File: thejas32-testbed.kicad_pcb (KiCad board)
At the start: 4 copper layers, 81.4 x 89.2 mm, 101 parts, among them J1 Conn_01x04, J10 Conn_02x10_Odd_Even, J11 Conn_01x03, J12 Conn_02x20_Odd_Even, J13 Conn_01x03, J2 USB_B_Micro, J3 Conn_02x03_Odd_Even, J4 Conn_02x05_Odd_Even, J5 Conn_01x05, J6 Conn_01x10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

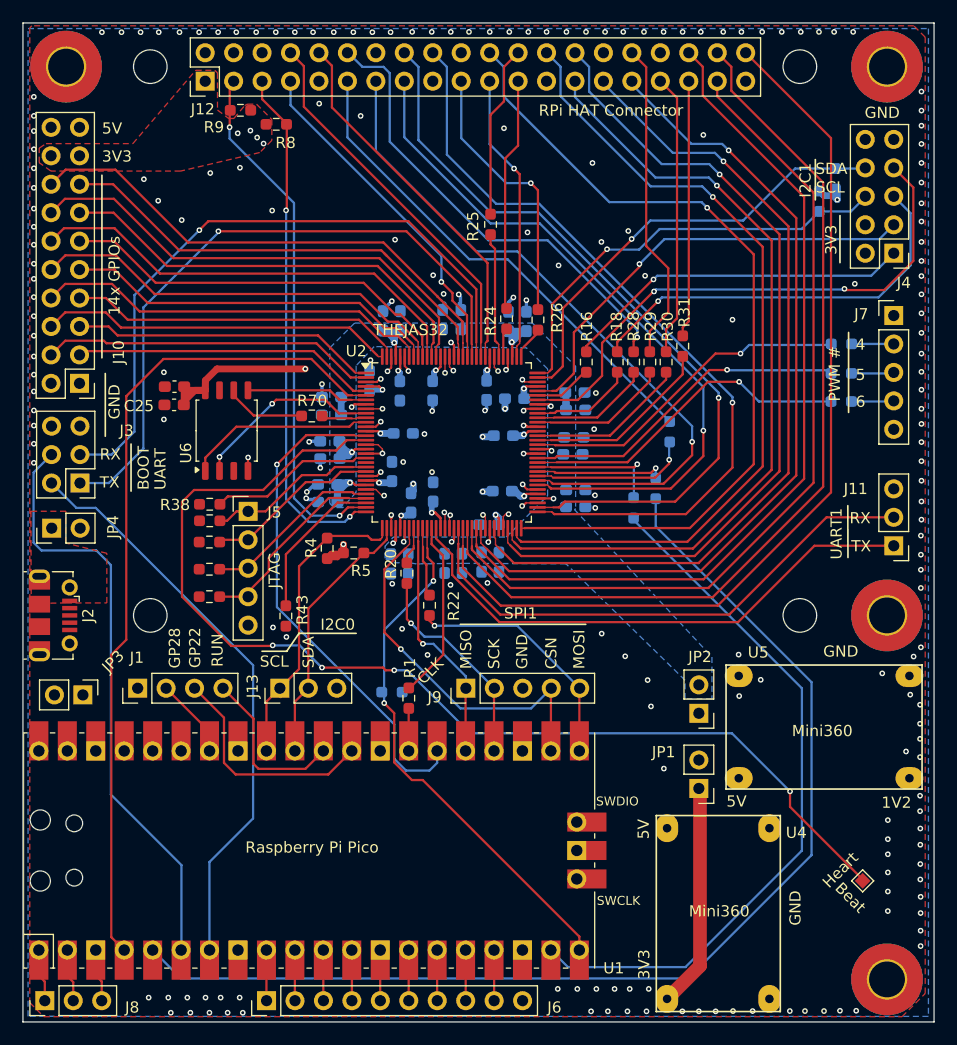
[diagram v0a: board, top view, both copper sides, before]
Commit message: Address review comments from Atharva
Various changes:
1. Deleted GND via near R9
2. Added vias near corner mounting holes
3. Thermal spoke width 40 mils for PWR_5V
   on 3rd layer
4. Fix square trace near J10.19
5. GND shapes on all planes - change to
   relief for PTH. Spoke width 20 mils
6. U1.26 routed trace above through-hole
   pafs
7. Improved routing of MCU_RESETN and
   HEARTBEAT for better GND shapes
8. U1.1-3 adjust traces to leave pad at
   90 degree

Plus silkscreen mods, including author,
version, name AtiVEGA and open hardware logo.
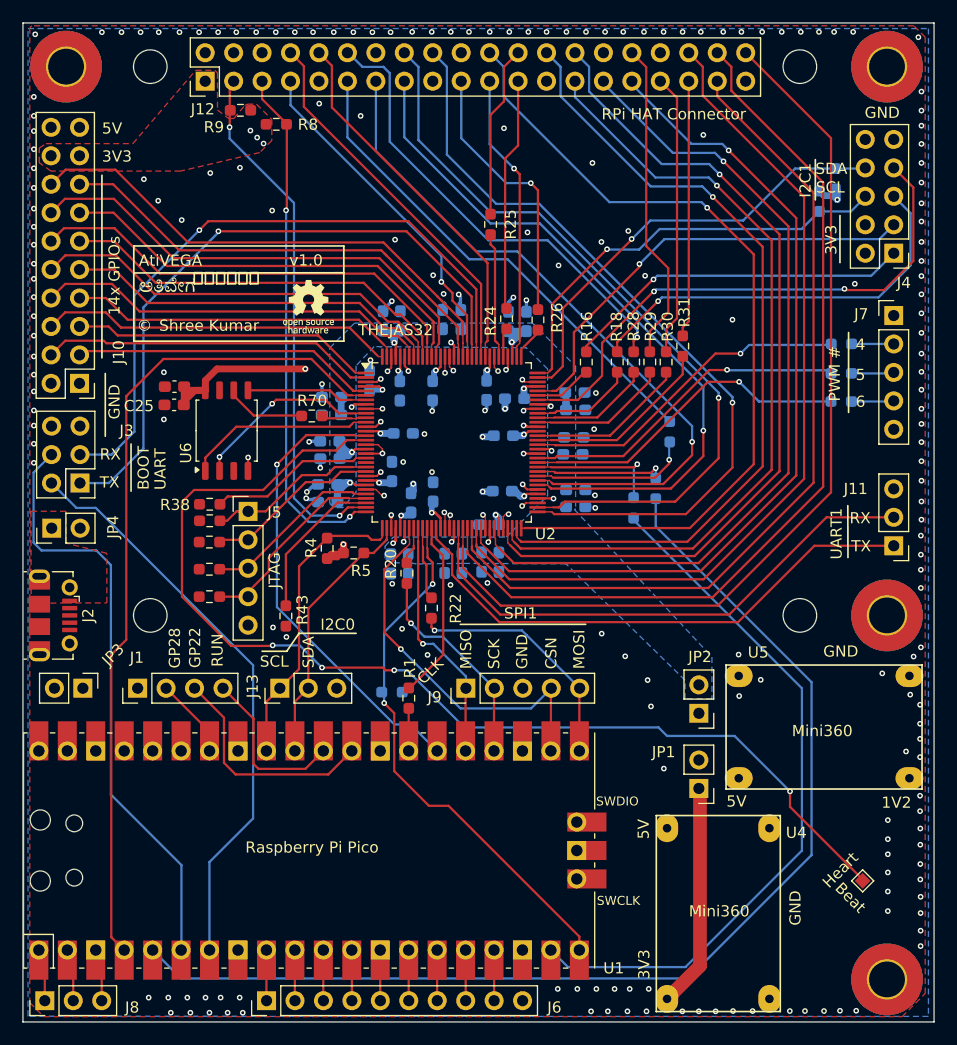
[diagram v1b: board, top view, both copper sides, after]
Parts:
- moved JP3 0.60 mm to (122.6, 126.0)
- moved R22 0.30 mm to (153.7, 118.8)
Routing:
- net MCU_BOOT_SEL: track 45.3 -> 41.4 mm
- net PWR_5V: track 140.8 -> 144.1 mm
- net Net-(JP3-B): track 5.58 -> 6.18 mm
- net GND: vias 232 -> 233
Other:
- board text added: "AtiVEGA"
- board text added: "Shree Kumar"
- board text added: "v1.0"
- board text added: "©"
- board text added: "ಅತಿವೇಗ"

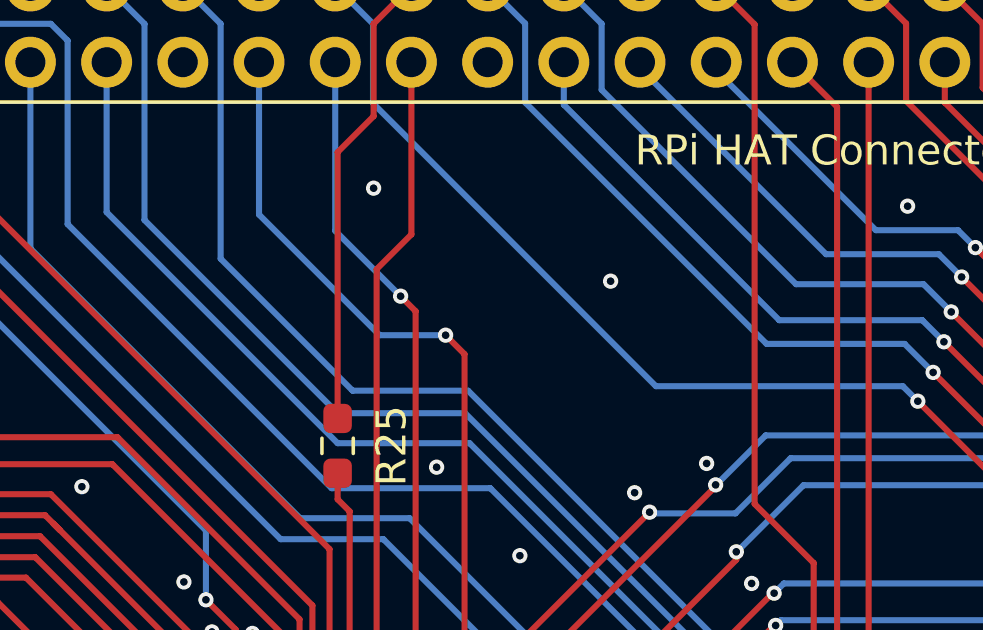
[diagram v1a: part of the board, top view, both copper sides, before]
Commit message: PCB and Silkscreen improvements
Added a couple of vias to create grounds between
traces. Moved a couple of traces to improve ground
near Pico.

Added github link as QR code on bottom silk
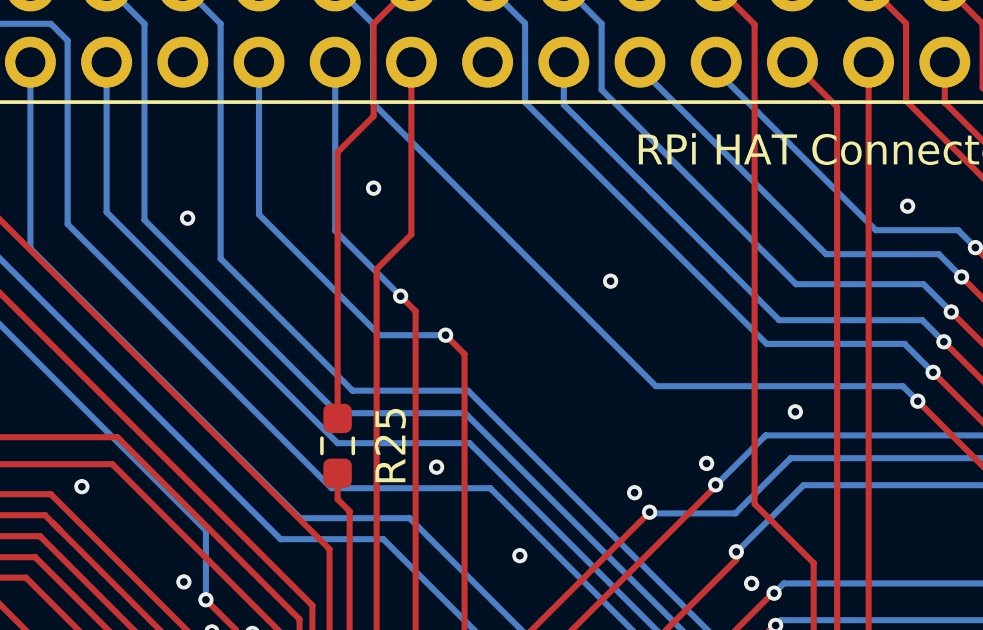
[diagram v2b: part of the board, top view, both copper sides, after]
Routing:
- net GND: vias 233 -> 235
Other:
- board text removed: "BOOT_SEL"

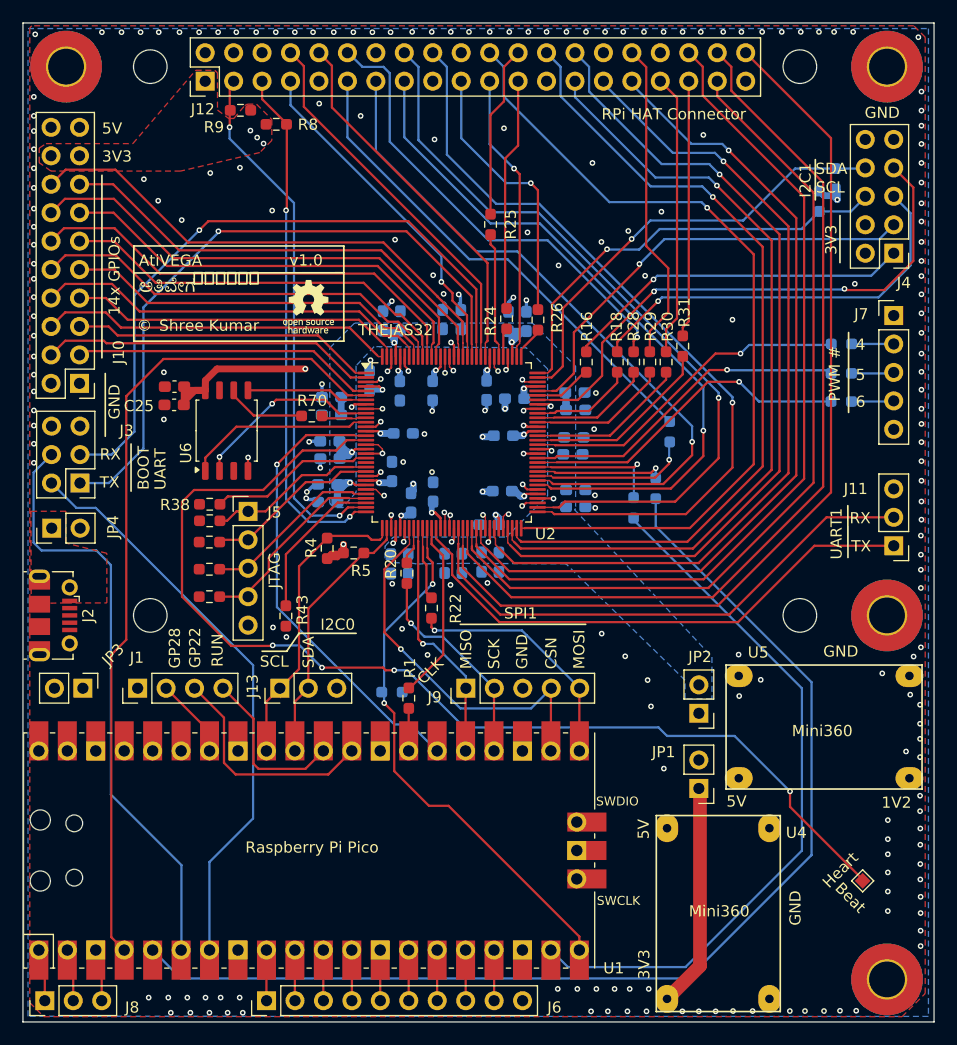
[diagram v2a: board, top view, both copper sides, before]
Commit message: Aligned with JLCPCB
0 DRC errors, 4 warnings.

Impedance matching on board - selected layer stackup on JLCPCB
is JLC04161H-3313. So, 6 mil traces have 50 ohm impedance.
Changed all 8 mil traces to 6 mils now. There are no "breakout"
traces - as everything is normalized to 6 mils. Existing 5 and
5.5 mil traces also promoted to 6 mils.

Board constraints are set to minimum clearance 5 mils, trace
width 6 mils. If you set minimum clearance to 6 mils, you'll see
DRC error on almost all THEJAS32 pads, complaining of "actual
clearance 5.92 mils, expected 6 mils". KiCAD doesn't seem to
honour fractional values, so I have to set it to 5 mils to pass.

Misc other changes:
1. USB connector is set up as "through-hole component". It was set
   to SMD earlier
2. Fix power plane supplying 5V to USB connector.
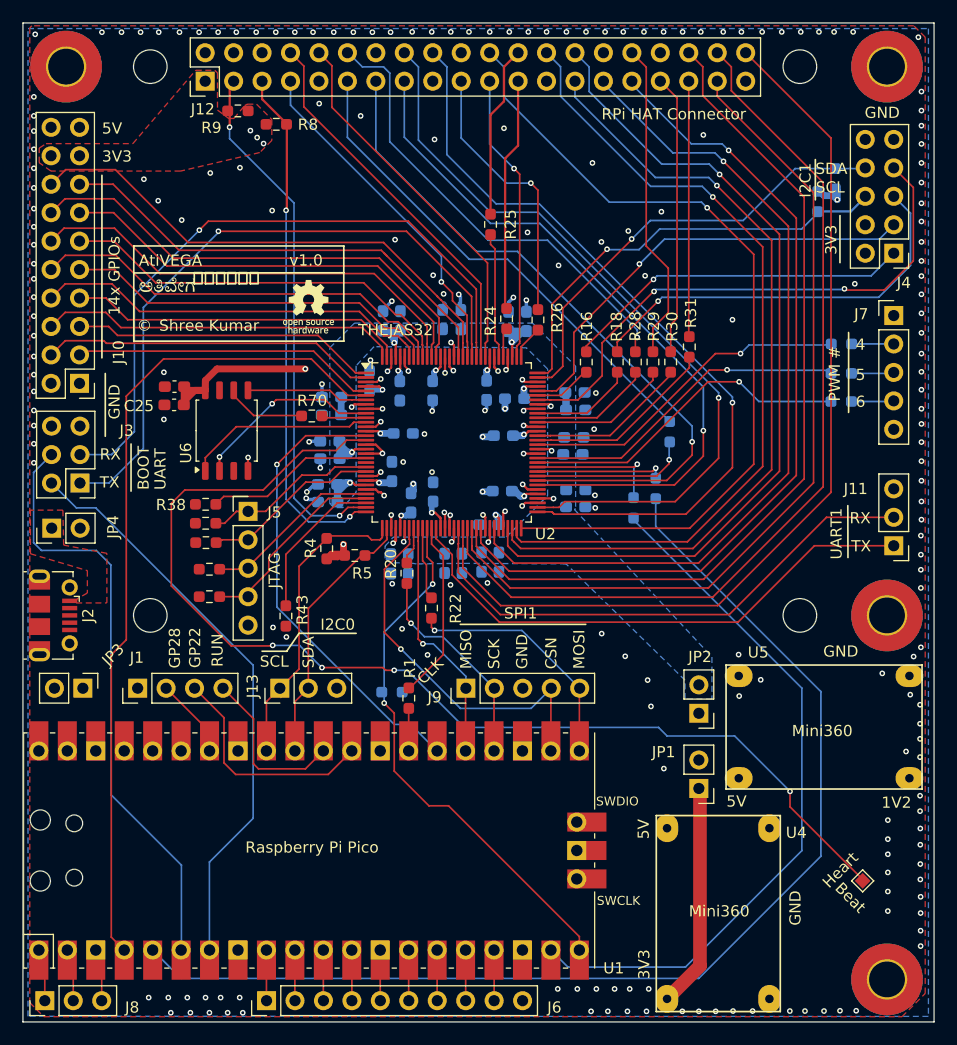
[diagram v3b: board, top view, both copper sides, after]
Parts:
- moved R31 0.59 mm to (176.8, 95.5)
- moved R39 0.43 mm to (133.6, 111.3)
- moved R30 0.41 mm to (175.1, 96.9)
- moved R38 0.36 mm to (133.6, 109.6)
- moved R40 0.32 mm to (133.6, 113.0)
- moved R29 0.28 mm to (173.5, 96.9)
- moved R5 0.25 mm to (146.9, 114.1)
- moved R9 0.23 mm to (136.4, 74.5)
- moved R28 0.16 mm to (171.9, 96.9)
- moved R6 0.14 mm to (188.2, 82.5)
- moved R4 0.05 mm to (144.4, 113.5)
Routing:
- net GND: track 66.3 -> 64.8 mm
- net Net-(U2-PROC_HEART_BEAT): track 99.4 -> 100.6 mm
- net MCU_GPIO_00: track 102.0 -> 103.3 mm
- net RPi_COMPAT_I2C1_SCL: track 47.2 -> 46.6 mm

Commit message: Cleanup
Cleaned up a few 8 mils signal tracks

Used Tools | Cleanup Tracks & Vias... This cleans
up tracks in pads, merges linear tracks, etc.

Aligned JTAG resistors in a line.
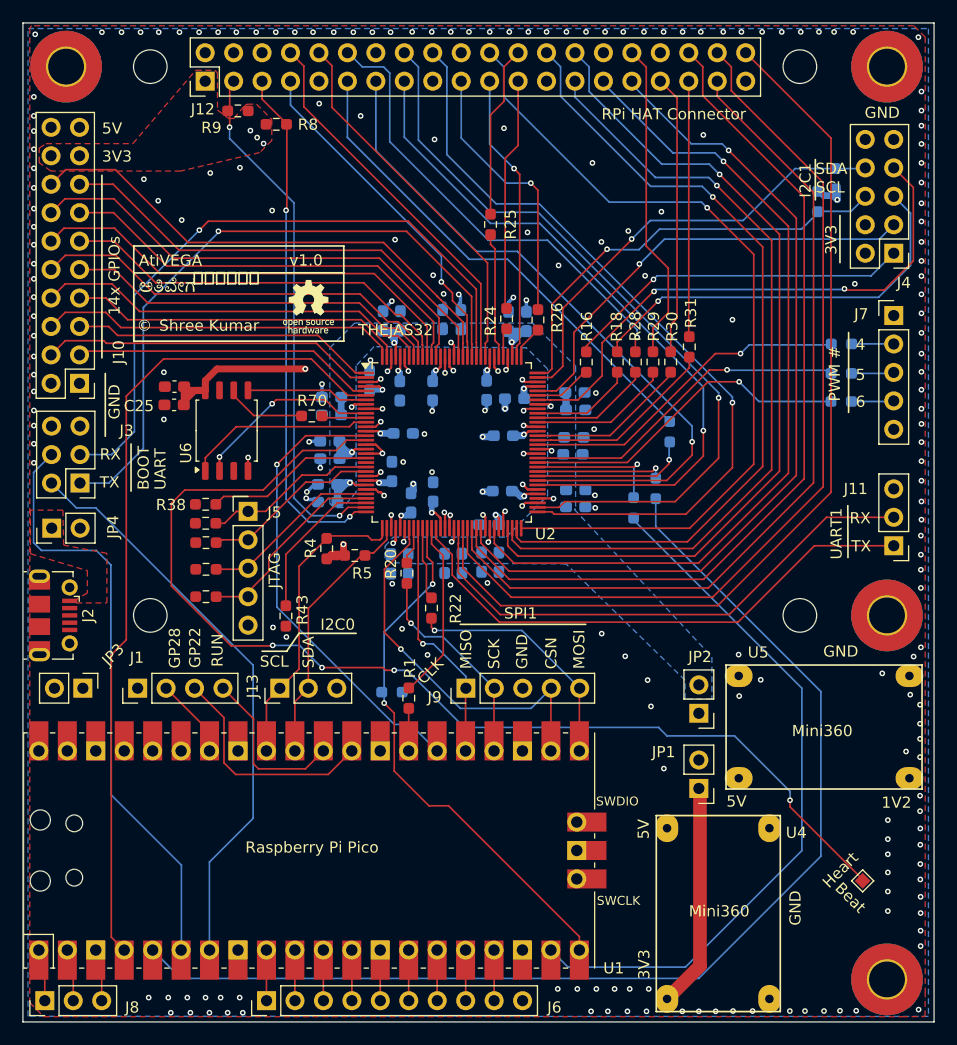
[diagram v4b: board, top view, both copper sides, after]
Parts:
- moved R42 0.31 mm to (133.6, 117.8)
- moved R41 0.31 mm to (133.6, 115.4)
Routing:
- net GND: track 64.8 -> 61.7 mm, vias 235 -> 236
- net Net-(J6-Pin_9): track 4.52 -> 1.98 mm
- net Net-(J6-Pin_8): track 4.52 -> 2.02 mm
- net Net-(J6-Pin_4): track 4.52 -> 2.08 mm
- net Net-(J1-Pin_2): track 7.21 -> 5.49 mm
- net PWR_3V3: track 177.9 -> 176.4 mm
- net Net-(J8-Pin_2): track 4.74 -> 3.99 mm
- net Net-(J8-Pin_1): track 4.74 -> 3.99 mm
- net PWR_5V: track 144.1 -> 143.5 mm
- net Net-(U2-SPI3_SCLK): track 4.28 -> 3.76 mm
- net Net-(U6-CLK): track 7.28 -> 6.75 mm
